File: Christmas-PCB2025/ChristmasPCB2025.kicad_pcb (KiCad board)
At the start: 2 copper layers, 20 parts, among them J1 Conn_01x08, Q1 2N7002_C306856

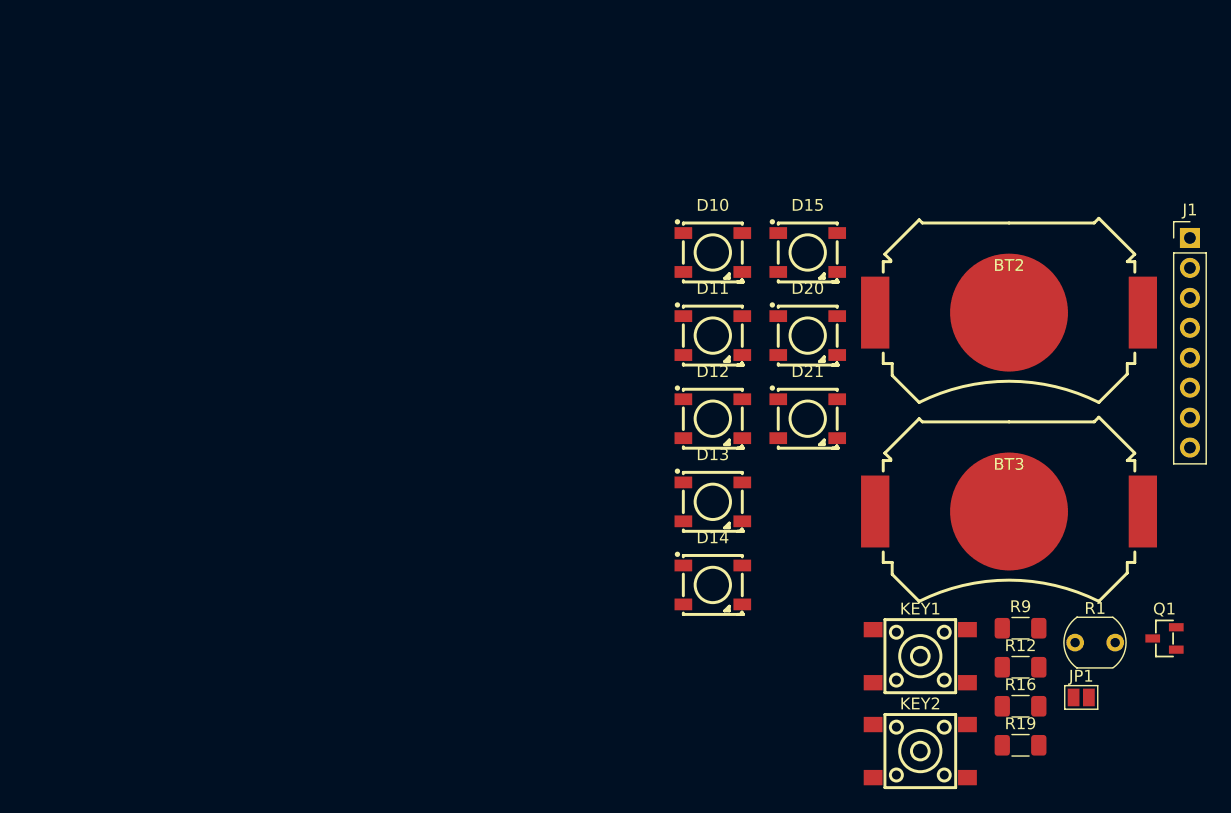
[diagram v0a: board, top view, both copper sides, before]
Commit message: removed many unnecessary components
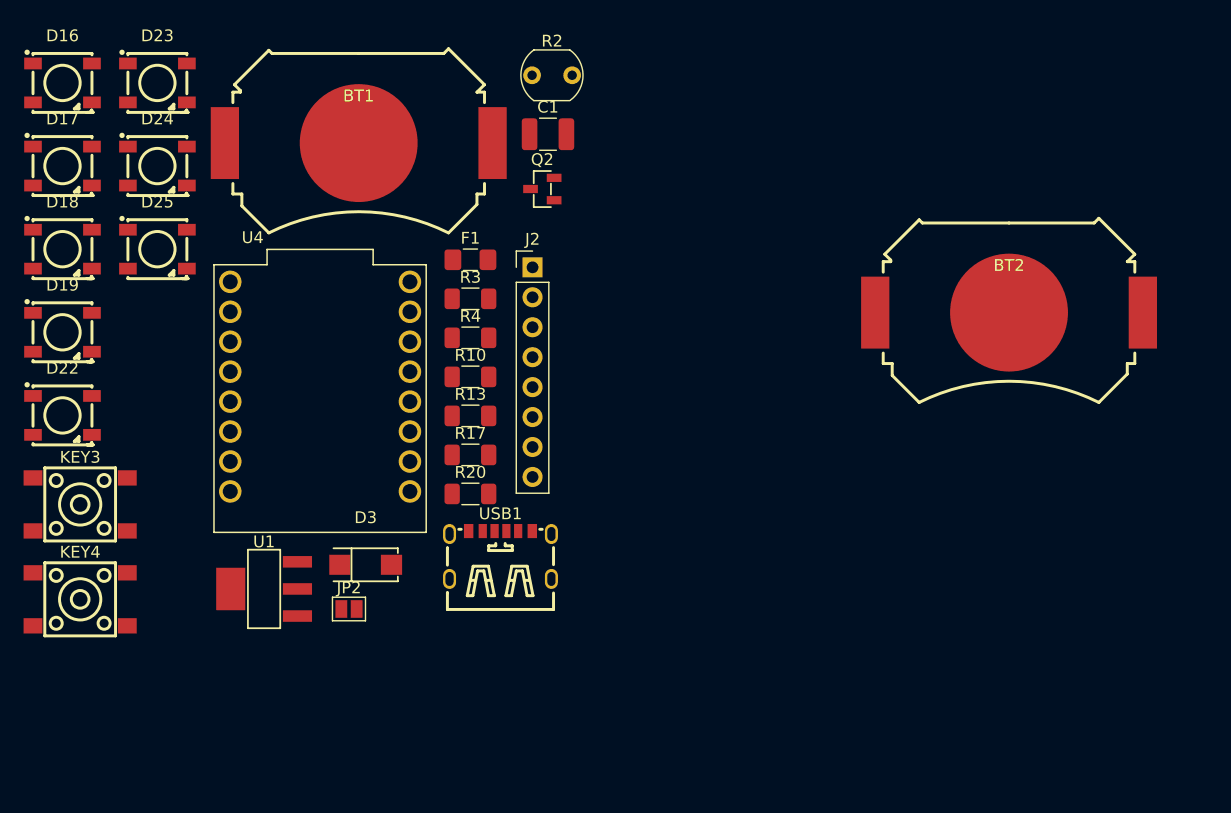
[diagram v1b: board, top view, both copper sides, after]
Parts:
- removed BT3: MY-2032-12, easyeda2kicad:BAT-SMD_MY-2032-12
- removed D10, D11, D12, D13, D14, D15, D20, D21: WS2812B, easyeda2kicad:LED-SMD_4P-L5.0-W5.0-BL_TC5050RGB
- removed J1: Conn_01x08, Connector_PinHeader_2.54mm:PinHeader_1x08_P2.54mm_Vertical
- removed JP1: SolderJumper_2_Open, Jumper:SolderJumper-2_P1.3mm_Open_Pad1.0x1.5mm
- removed KEY1, KEY2: DTSM-61R-V-T/R, easyeda2kicad:KEY-SMD_4P-L6.2-W6.2-P4.50-LS9.0
- removed Q1: 2N7002_C306856, easyeda2kicad:SOT-23-3_L2.9-W1.3-P1.90-LS2.4-BR
- removed R1: LDR07, OptoDevice:R_LDR_5.1x4.3mm_P3.4mm_Vertical
- removed R12, R19: 200, Resistor_SMD:R_1206_3216Metric_Pad1.30x1.75mm_HandSolder
- removed R16: 5k, Resistor_SMD:R_1206_3216Metric_Pad1.30x1.75mm_HandSolder
- removed R9: 10k, Resistor_SMD:R_1206_3216Metric_Pad1.30x1.75mm_HandSolder
- added BT1: MY-2032-12, easyeda2kicad:BAT-SMD_MY-2032-12, F.Cu at (44.2, 35.0)
- added C1: 47uF 10V, Capacitor_SMD:C_1210_3225Metric_Pad1.33x2.70mm_HandSolder, F.Cu at (60.2, 34.3)
- added D16: WS2812B, easyeda2kicad:LED-SMD_4P-L5.0-W5.0-BL_TC5050RGB, F.Cu at (19.0, 29.9)
- added D17: WS2812B, easyeda2kicad:LED-SMD_4P-L5.0-W5.0-BL_TC5050RGB, F.Cu at (19.0, 37.0)
- added D18: WS2812B, easyeda2kicad:LED-SMD_4P-L5.0-W5.0-BL_TC5050RGB, F.Cu at (19.0, 44.0)
- added D19: WS2812B, easyeda2kicad:LED-SMD_4P-L5.0-W5.0-BL_TC5050RGB, F.Cu at (19.0, 51.1)
- added D22: WS2812B, easyeda2kicad:LED-SMD_4P-L5.0-W5.0-BL_TC5050RGB, F.Cu at (19.0, 58.1)
- added D23: WS2812B, easyeda2kicad:LED-SMD_4P-L5.0-W5.0-BL_TC5050RGB, F.Cu at (27.1, 29.9)
- added D24: WS2812B, easyeda2kicad:LED-SMD_4P-L5.0-W5.0-BL_TC5050RGB, F.Cu at (27.1, 37.0)
- added D25: WS2812B, easyeda2kicad:LED-SMD_4P-L5.0-W5.0-BL_TC5050RGB, F.Cu at (27.1, 44.0)
- added D3: 1N5819_C437199, easyeda2kicad:SMA_L4.4-W2.6-LS5.0-RD, F.Cu at (44.7, 70.8)
- added F1: Fuse_Small 2A, Fuse:Fuse_1206_3216Metric_Pad1.42x1.75mm_HandSolder, F.Cu at (53.6, 44.9)
- added J2: Conn_01x08, Connector_PinHeader_2.54mm:PinHeader_1x08_P2.54mm_Vertical, F.Cu at (58.9, 45.6)
- added JP2: SolderJumper_2_Open, Jumper:SolderJumper-2_P1.3mm_Open_Pad1.0x1.5mm, F.Cu at (43.3, 74.5)
- added KEY3: DTSM-61R-V-T/R, easyeda2kicad:KEY-SMD_4P-L6.2-W6.2-P4.50-LS9.0, F.Cu at (20.5, 65.7)
- added KEY4: DTSM-61R-V-T/R, easyeda2kicad:KEY-SMD_4P-L6.2-W6.2-P4.50-LS9.0, F.Cu at (20.5, 73.7)
- added Q2: 2N7002_C306856, easyeda2kicad:SOT-23-3_L2.9-W1.3-P1.90-LS2.4-BR, F.Cu at (59.7, 38.9)
- added R10: 10k, Resistor_SMD:R_1206_3216Metric_Pad1.30x1.75mm_HandSolder, F.Cu at (53.6, 54.9)
- added R13: 200, Resistor_SMD:R_1206_3216Metric_Pad1.30x1.75mm_HandSolder, F.Cu at (53.6, 58.2)
- added R17: 5k, Resistor_SMD:R_1206_3216Metric_Pad1.30x1.75mm_HandSolder, F.Cu at (53.6, 61.5)
- added R2: LDR07, OptoDevice:R_LDR_5.1x4.3mm_P3.4mm_Vertical, F.Cu at (58.9, 29.3)
- added R20: 200, Resistor_SMD:R_1206_3216Metric_Pad1.30x1.75mm_HandSolder, F.Cu at (53.6, 64.8)
- added R3: 5k1, Resistor_SMD:R_1206_3216Metric_Pad1.30x1.75mm_HandSolder, F.Cu at (53.6, 48.2)
- added R4: 5k1, Resistor_SMD:R_1206_3216Metric_Pad1.30x1.75mm_HandSolder, F.Cu at (53.6, 51.5)
- added U1: AMS1117-3.3_C347222, easyeda2kicad:SOT-223-4_L6.5-W3.5-P2.30-LS7.0-BR, F.Cu at (36.1, 72.8)
- added U4: ESP32-C3_SUPERMINI_TH, custom:MODULE_ESP32-C3_SUPERMINI, F.Cu at (40.9, 56.7)
- added USB1: TYPE-C 6P(073), easyeda2kicad:TYPE-C-SMD_TYPE-C-6P_5, F.Cu at (56.2, 70.0)
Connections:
- BT2 pad 1: +5V -> Net-(BT1-Pad2)
- BT2 pad 2: Net-(BT2-Pad2) -> GND

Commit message: added new design types
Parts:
- removed D16, D17, D18, D19, D22, D23, D24, D25: WS2812B, easyeda2kicad:LED-SMD_4P-L5.0-W5.0-BL_TC5050RGB
- removed J2: Conn_01x08, Connector_PinHeader_2.54mm:PinHeader_1x08_P2.54mm_Vertical
- removed JP2: SolderJumper_2_Open, Jumper:SolderJumper-2_P1.3mm_Open_Pad1.0x1.5mm
- removed KEY3, KEY4: DTSM-61R-V-T/R, easyeda2kicad:KEY-SMD_4P-L6.2-W6.2-P4.50-LS9.0
- removed Q2: 2N7002_C306856, easyeda2kicad:SOT-23-3_L2.9-W1.3-P1.90-LS2.4-BR
- removed R13, R20: 200, Resistor_SMD:R_1206_3216Metric_Pad1.30x1.75mm_HandSolder
- removed R17: 5k, Resistor_SMD:R_1206_3216Metric_Pad1.30x1.75mm_HandSolder
- removed U4: ESP32-C3_SUPERMINI_TH, custom:MODULE_ESP32-C3_SUPERMINI
- removed USB1: TYPE-C 6P(073), easyeda2kicad:TYPE-C-SMD_TYPE-C-6P_5
- added BATT+: ~, TestPoint:TestPoint_Pad_D3.0mm, F.Cu at (407.5, 89.2)
- added BATT+1: ~, TestPoint:TestPoint_Pad_D3.0mm, F.Cu at (87.9, 18.9)
- added BATT-: TestPoint_Alt, TestPoint:TestPoint_Pad_D3.0mm, F.Cu at (414.1, 89.2)
- added BATT-1: TestPoint_Alt, TestPoint:TestPoint_Pad_D3.0mm, F.Cu at (87.9, 23.9)
- added BATTPACK1, BATTPACK2: Batteryplaceholder, MountingHole:MountingHole_2.1mm, F.Cu at (338.5, 67.8)
- added BUTTON1: DTSM-61R-V-T/R, easyeda2kicad:KEY-SMD_4P-L6.2-W6.2-P4.50-LS9.0, B.Cu at (410.1, 75.9)
- added BUTTON2: DTSM-61R-V-T/R, easyeda2kicad:KEY-SMD_4P-L6.2-W6.2-P4.50-LS9.0, B.Cu at (305.2, 66.6)
- added C2: 47uF 10V, Capacitor_SMD:C_1210_3225Metric_Pad1.33x2.70mm_HandSolder, F.Cu at (386.7, 117.4)
- added C3: 100nF 50V, Capacitor_SMD:C_1210_3225Metric_Pad1.33x2.70mm_HandSolder, F.Cu at (382.1, 117.4)
- added C4: 10uF 25V, Capacitor_SMD:C_1210_3225Metric_Pad1.33x2.70mm_HandSolder, F.Cu at (382.0, 110.5)
- added D1: SM712_SOT23, Package_TO_SOT_SMD:SOT-23, F.Cu at (87.6, 32.0)
- added D3: SM712_SOT23, Package_TO_SOT_SMD:SOT-23, F.Cu at (380.6, 91.8)
- added D4: SM712_SOT23, Package_TO_SOT_SMD:SOT-23, F.Cu at (377.6, 93.7)
- added D5: 1N5819_C437199, easyeda2kicad:SMA_L4.4-W2.6-LS5.0-RD, F.Cu at (400.7, 103.0)
- added F2: Fuse_Small 2A, Fuse:Fuse_1206_3216Metric_Pad1.42x1.75mm_HandSolder, F.Cu at (398.9, 109.2)
- added G***: LOGO, project_footprints:tree_shadow, F.Cu at (430.3, -91.6)
- added G***: LOGO, project_footprints:frosty-shadow, F.Cu at (280.5, -74.6)
- added G***: LOGO, project_footprints:frosty-body, F.Cu at (280.8, -75.0)
- added G***: LOGO, project_footprints:frosty-carrot, F.Cu at (281.0, -75.6)
- added G***: LOGO, project_footprints:ornament_reflect, F.Cu at (137.9, -70.6)
- added G***: LOGO, project_footprints:tree_star, F.Cu at (428.5, -98.4)
- added G***: LOGO, project_footprints:ornament_shadow, F.Cu at (135.4, -68.7)
- added G***: LOGO, project_footprints:ornament_crown, F.Cu at (135.1, -69.5)
- added GND: TestPoint_Probe, TestPoint:TestPoint_Pad_D2.0mm, F.Cu at (358.5, 92.0)
- added HDR1: Conn_01x08, Connector_PinHeader_2.54mm:PinHeader_1x08_P2.54mm_Vertical, B.Cu at (401.5, 73.0)
- added J1: Conn_01x08, Connector_PinHeader_2.54mm:PinHeader_1x08_P2.54mm_Vertical_SMD_Pin1Left, F.Cu at (75.5, 27.6)
- added JP1: SolderJumper_2_Open, Jumper:SolderJumper-2_P1.3mm_Open_Pad1.0x1.5mm, F.Cu at (87.3, 36.0)
- added LDR1: LDR07, OptoDevice:R_LDR_5.1x4.3mm_P3.4mm_Vertical, B.Cu at (397.8, 60.9)
- added LED1: WS2812B, easyeda2kicad:LED-SMD_4P-L5.0-W5.0-BL_TC5050RGB, B.Cu at (386.9, 32.6)
- added LED2: WS2812B, easyeda2kicad:LED-SMD_4P-L5.0-W5.0-BL_TC5050RGB, B.Cu at (337.2, 33.5)
- added LED3: WS2812B, easyeda2kicad:LED-SMD_4P-L5.0-W5.0-BL_TC5050RGB, B.Cu at (409.5, 64.7)
- added LED4: WS2812B, easyeda2kicad:LED-SMD_4P-L5.0-W5.0-BL_TC5050RGB, B.Cu at (308.9, 51.7)
- added LED5: WS2812B, easyeda2kicad:LED-SMD_4P-L5.0-W5.0-BL_TC5050RGB, B.Cu at (407.3, 97.0)
- added LED6: WS2812B, easyeda2kicad:LED-SMD_4P-L5.0-W5.0-BL_TC5050RGB, B.Cu at (307.0, 83.5)
- added LED7: WS2812B, easyeda2kicad:LED-SMD_4P-L5.0-W5.0-BL_TC5050RGB, B.Cu at (379.3, 110.5)
- added LED8: WS2812B, easyeda2kicad:LED-SMD_4P-L5.0-W5.0-BL_TC5050RGB, B.Cu at (346.6, 108.4)
- added LS1: KSSGK4B16-20, CustomPartsCRT:KSSGK4B16-20, B.Cu at (349.8, 57.5)
- added Q1: 2N7002_C306856, easyeda2kicad:SOT-23-3_L2.9-W1.3-P1.90-LS2.4-BR, F.Cu at (109.0, 129.0)
- added R11: 200, Resistor_SMD:R_1206_3216Metric_Pad1.30x1.75mm_HandSolder, F.Cu at (107.3, 134.9)
- added R12: 10k, Resistor_SMD:R_1206_3216Metric_Pad1.30x1.75mm_HandSolder, F.Cu at (110.7, 134.9)
- added R14: 200, Resistor_SMD:R_1206_3216Metric_Pad1.30x1.75mm_HandSolder, F.Cu at (353.2, 112.0)
- added R15: 10k, Resistor_SMD:R_1206_3216Metric_Pad1.30x1.75mm_HandSolder, F.Cu at (388.2, 111.4)
- added R2: 10k, Resistor_SMD:R_1206_3216Metric_Pad1.30x1.75mm_HandSolder, F.Cu at (82.4, 18.0)
- added R4: 10k, Resistor_SMD:R_1206_3216Metric_Pad1.30x1.75mm_HandSolder, F.Cu at (82.4, 24.6)
- added R5: 100, Resistor_SMD:R_1206_3216Metric_Pad1.30x1.75mm_HandSolder, F.Cu at (82.4, 27.9)
- added R8: 5k, Resistor_SMD:R_1206_3216Metric_Pad1.30x1.75mm_HandSolder, F.Cu at (396.0, 66.0)
- added R9: 10k, Resistor_SMD:R_1206_3216Metric_Pad1.30x1.75mm_HandSolder, F.Cu at (111.2, 119.9)
- added REF**: Pin_Header_Straight_1x01, idlehands_footprints:frosty-eye, F.Cu at (288.4, -98.9)
- added REF**: MountingHole_2.5mm, idlehands_footprints:MountingHole_2.5mm_NO, B.Cu at (135.1, -113.0)
- added REF**: MountingHole_2.5mm, idlehands_footprints:MountingHole_2.5mm_NO, B.Cu at (280.7, -124.6)
- added REF**: MountingHole_2.5mm, idlehands_footprints:MountingHole_2.5mm_NO, B.Cu at (428.7, -142.0)
- added RXD: TestPoint_Probe, TestPoint:TestPoint_Pad_D2.0mm, F.Cu at (354.4, 92.0)
- added TXD: TestPoint_Probe, TestPoint:TestPoint_Pad_D2.0mm, F.Cu at (350.4, 91.9)
- added USB+: TestPoint_Probe, TestPoint:TestPoint_Pad_D2.0mm, F.Cu at (365.7, 94.6)
- added USB-: TestPoint_Probe, TestPoint:TestPoint_Pad_D2.0mm, F.Cu at (370.8, 94.6)
- D1: renamed from D3; value 1N5819_C437199 -> WS2812B
- F1: value Fuse_Small 2A -> Resetable fuse 0.75A
- R1: renamed from R2; value LDR07 -> 10k; footprint OptoDevice:R_LDR_5.1x4.3mm_P3.4mm_Vertical -> Resistor_SMD:R_1206_3216Metric_Pad1.30x1.75mm_HandSolder
- R3: value 5k1 -> 200
- R7: renamed from R4; value 5k1 -> 5k
- U1: value AMS1117-3.3_C347222 -> ESP32-C3_SUPERMINI_TH; footprint easyeda2kicad:SOT-223-4_L6.5-W3.5-P2.30-LS7.0-BR -> custom:MODULE_ESP32-C3_SUPERMINI
- moved C1 339.2 mm to (392.2, 103.5), turned to 180 degrees
- moved BT1 309.1 mm to (351.6, 66.6), turned to 180 degrees
- moved BT2 278.7 mm to (377.5, 66.6), turned to 180 degrees
- moved U1 243.9 mm to (274.2, 126.2)
- moved R10 84.2 mm to (107.0, 119.9), turned to -90 degrees
- moved R3 39.4 mm to (82.4, 21.3)
- moved D1 21.6 mm to (66.3, 70.5)
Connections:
- BT1 pad 1: Net-(D3-A) -> Net-(BT1-Pad2)
- BT1 pad 2: Net-(BT1-Pad2) -> GND
- BT2 pad 1: Net-(BT1-Pad2) -> Net-(D1-A)
- BT2 pad 2: GND -> Net-(BT1-Pad2)
- D1 pad 1: Net-(D3-C) -> +5V
- D1 pad 2: Net-(D3-A) -> Net-(D3-DOUT)
- F1 pad 2: Net-(D3-C) -> Net-(D1-C)
- R1 pad 1: +3V3 -> BATT_V
- R1 pad 2: Net-(U4-GPIO2) -> GND
- R10 pad 1: GND -> Net-(D1-A)
- R10 pad 2: BUZZ -> BATT_V
- R3 pad 1: GND -> Net-(D2-DIN)
- R3 pad 2: Net-(USB1-CC2) -> RGB
- R7 pad 1: GND -> Net-(U1-GPIO2)
- R7 pad 2: Net-(USB1-CC1) -> GND
- U1 pad 1: +3V3 -> unconnected-(U1-GPIO1-Pad1)
- U1 pad 2: +3V3 -> Net-(U1-GPIO2)
- U1 pad 3: +5V -> unconnected-(U1-GPIO3-Pad3)
- U1 pad 4: GND -> Net-(U1-GPIO4)
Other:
- board outline added: 388.8 x 303.7 mm
- board text added: "3.3V"
- board text added: "AAA"
- board text added: "BATTERY_V"
- board text added: "BUZZER_CTRL"
- board text added: "CR2032"
- board text added: "GND"
- board text added: "GPIO HDR"
- board text added: "INT"
- board text added: "Mounting Hole"
- board text added: "NC"
- board text added: "SCL"
- board text added: "SDA"
- board text added: "SDO"
- board text added: "Wear me! Mount me! Stand me! Dangle me!"

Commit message: settled on ornament design
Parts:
- removed BATT+: ~, TestPoint:TestPoint_Pad_D3.0mm
- removed BATT-: TestPoint_Alt, TestPoint:TestPoint_Pad_D3.0mm
- removed BATTPACK2: Batteryplaceholder, MountingHole:MountingHole_2.1mm
- removed C1, C2: 47uF 10V, Capacitor_SMD:C_1210_3225Metric_Pad1.33x2.70mm_HandSolder
- removed C3: 100nF 50V, Capacitor_SMD:C_1210_3225Metric_Pad1.33x2.70mm_HandSolder
- removed C4: 10uF 25V, Capacitor_SMD:C_1210_3225Metric_Pad1.33x2.70mm_HandSolder
- removed D3, D4: SM712_SOT23, Package_TO_SOT_SMD:SOT-23
- removed D5: 1N5819_C437199, easyeda2kicad:SMA_L4.4-W2.6-LS5.0-RD
- removed F2: Fuse_Small 2A, Fuse:Fuse_1206_3216Metric_Pad1.42x1.75mm_HandSolder
- removed the G*** at (430.3, -91.6)
- removed the G*** at (280.5, -74.6)
- removed the G*** at (280.8, -75.0)
- removed the G*** at (281.0, -75.6)
- removed the G*** at (428.5, -98.4)
- removed GND, RXD, TXD, USB+, USB-: TestPoint_Probe, TestPoint:TestPoint_Pad_D2.0mm
- removed HDR1: Conn_01x08, Connector_PinHeader_2.54mm:PinHeader_1x08_P2.54mm_Vertical
- removed R10, R12, R15, R9: 10k, Resistor_SMD:R_1206_3216Metric_Pad1.30x1.75mm_HandSolder
- removed R11, R14: 200, Resistor_SMD:R_1206_3216Metric_Pad1.30x1.75mm_HandSolder
- removed R8: 5k, Resistor_SMD:R_1206_3216Metric_Pad1.30x1.75mm_HandSolder
- removed the REF** at (288.4, -98.9)
- removed the REF** at (135.1, -113.0)
- removed the REF** at (280.7, -124.6)
- removed the REF** at (428.7, -142.0)
- added BATTPACK1: Batteryplaceholder, MountingHole:MountingHole_2.1mm, B.Cu at (160.0, -66.8)
- added D2: SM712_SOT23, Package_TO_SOT_SMD:SOT-23, F.Cu at (197.9, -79.5)
- added REF**: MountingHole_2.5mm, idlehands_footprints:MountingHole_2.5mm_NO, B.Cu at (135.1, -112.8)
- D1: value WS2812B -> 1N5819_C437199
- D1: value SM712_SOT23 -> 1N5819_C437199
- U1: moved to B.Cu
- moved LED2 230.0 mm to (144.4, -91.8), turned to 180 degrees
- moved U1 214.1 mm to (135.0, -36.5)
- moved G*** 0.26 mm to (135.1, -69.2)
- moved G*** 0.26 mm to (137.9, -70.3)
- moved G*** 0.26 mm to (135.4, -68.5)
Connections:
- BT1 pad 1: Net-(BT1-Pad2) -> Net-(D1-A)
- BT1 pad 2: GND -> Net-(BT1-Pad2)
- BT2 pad 1: Net-(D1-A) -> Net-(BT1-Pad2)
- BT2 pad 2: Net-(BT1-Pad2) -> GND
- BUTTON1 pad 3: GPIO4 -> Net-(U1-GPIO4)
- BUTTON1 pad 4: GPIO4 -> Net-(U1-GPIO4)
- BUTTON2 pad 3: GPIO5 -> Net-(U1-GPIO5)
- BUTTON2 pad 4: GPIO5 -> Net-(U1-GPIO5)
- D1 pad 1: +5V -> Net-(D1-C)
- D1 pad 2: Net-(D3-DOUT) -> Net-(D1-A)
- D1 pad 1: SCL -> Net-(D1-C)
- D1 pad 2: SDA -> Net-(D1-A)
- D1 pad 3: GND -> (no net)
- LDR1 pad 2: Net-(U2-IO2) -> Net-(U1-GPIO2)
- LED1 pad 2: Net-(LED5-DOUT) -> Net-(LED1-DOUT)
- LED1 pad 4: Net-(LED4-DOUT) -> Net-(LED1-DIN)
- LED2 pad 2: Net-(LED4-DOUT) -> Net-(LED2-DOUT)
- LED2 pad 4: Net-(LED3-DOUT) -> Net-(LED1-DOUT)
- LED3 pad 2: Net-(LED6-DOUT) -> Net-(LED3-DOUT)
- LED3 pad 4: Net-(LED5-DOUT) -> Net-(LED2-DOUT)
- LED4 pad 2: Net-(LED3-DOUT) -> Net-(LED4-DOUT)
- LED4 pad 4: Net-(LED2-DOUT) -> Net-(LED3-DOUT)
- LED5 pad 2: Net-(LED7-DOUT) -> Net-(LED5-DOUT)
- LED5 pad 4: Net-(LED6-DOUT) -> Net-(LED4-DOUT)
- LED6 pad 2: Net-(LED2-DOUT) -> Net-(LED6-DOUT)
- LED6 pad 4: Net-(LED1-DOUT) -> Net-(LED5-DOUT)
- LED7 pad 2: unconnected-(LED8-DOUT-Pad2) -> Net-(LED7-DOUT)
- LED7 pad 4: Net-(LED7-DOUT) -> Net-(LED6-DOUT)
- LED8 pad 2: Net-(LED1-DOUT) -> unconnected-(LED8-DOUT-Pad2)
- LED8 pad 4: Net-(LED1-DIN) -> Net-(LED7-DOUT)
- R3 pad 1: Net-(D2-DIN) -> Net-(LED1-DIN)
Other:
- board size 388.8 x 303.7 mm -> 134.3 x 272.6 mm

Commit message: finished playfull routing
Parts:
- removed BATTPACK1: Batteryplaceholder, MountingHole:MountingHole_2.1mm
- removed BT1, BT2: MY-2032-12, easyeda2kicad:BAT-SMD_MY-2032-12
- removed the D1 at (87.6, 32.0)
- removed D2: SM712_SOT23, Package_TO_SOT_SMD:SOT-23
- removed J1: Conn_01x08, Connector_PinHeader_2.54mm:PinHeader_1x08_P2.54mm_Vertical_SMD_Pin1Left
- BATT+: renamed from BATT+1; moved to B.Cu
- BATT-: renamed from BATT-1; moved to B.Cu
- D1, F1, JP1, Q1, R1, R2, R3, R4, R5, R7: moved to B.Cu
- LED1: renamed from LED2; footprint easyeda2kicad:LED-SMD_4P-L5.0-W5.0-BL_TC5050RGB -> CustomLed:LED_WS2812B_PLCC4_5.0x5.0mm_P3.2mm
- LED2: renamed from LED4; footprint easyeda2kicad:LED-SMD_4P-L5.0-W5.0-BL_TC5050RGB -> CustomLed:LED_WS2812B_PLCC4_5.0x5.0mm_P3.2mm
- LED3, LED6: footprint easyeda2kicad:LED-SMD_4P-L5.0-W5.0-BL_TC5050RGB -> CustomLed:LED_WS2812B_PLCC4_5.0x5.0mm_P3.2mm
- LED4: renamed from LED8; footprint easyeda2kicad:LED-SMD_4P-L5.0-W5.0-BL_TC5050RGB -> CustomLed:LED_WS2812B_PLCC4_5.0x5.0mm_P3.2mm
- LED5: renamed from LED7; footprint easyeda2kicad:LED-SMD_4P-L5.0-W5.0-BL_TC5050RGB -> CustomLed:LED_WS2812B_PLCC4_5.0x5.0mm_P3.2mm
- LED7: renamed from LED5; footprint easyeda2kicad:LED-SMD_4P-L5.0-W5.0-BL_TC5050RGB -> CustomLed:LED_WS2812B_PLCC4_5.0x5.0mm_P3.2mm
- LED8: renamed from LED1; footprint easyeda2kicad:LED-SMD_4P-L5.0-W5.0-BL_TC5050RGB -> CustomLed:LED_WS2812B_PLCC4_5.0x5.0mm_P3.2mm
- moved LDR1 273.6 mm to (125.0, 82.8), turned to -140 degrees
- moved LED3 267.8 mm to (146.1, 113.0)
- moved LED5 263.3 mm to (116.0, 113.9)
- moved LED8 250.5 mm to (140.7, 79.2)
- moved LED7 248.1 mm to (161.4, 130.2)
- moved BUTTON1 237.1 mm to (174.0, 97.7)
- moved LED4 214.7 mm to (132.1, 98.4)
- moved LS1 199.6 mm to (151.6, 81.0), turned to -90 degrees
- moved BUTTON2 193.5 mm to (114.2, 97.6)
- moved LED6 186.8 mm to (126.4, 131.5), turned to 150 degrees
- moved LED1 182.2 mm to (162.0, 89.5)
- moved BATTPACK1: 172.3 mm to (169.7, 105.2)
- moved G*** 172.2 mm to (144.2, 103.5)
- moved G*** 172.2 mm to (143.9, 102.7)
- moved G*** 172.2 mm to (146.7, 101.7)
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- renumbered BATTPACK1 to BATTPACK1:
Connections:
- net SCL renamed Net-(JP1-B)
- LED1 pad 2: Net-(LED2-DOUT) -> Net-(LED1-DOUT)
- LED1 pad 4: Net-(LED1-DOUT) -> Net-(LED1-DIN)
- LED2 pad 2: Net-(LED4-DOUT) -> Net-(LED2-DOUT)
- LED2 pad 4: Net-(LED3-DOUT) -> Net-(LED1-DOUT)
- LED4 pad 2: unconnected-(LED8-DOUT-Pad2) -> Net-(LED4-DOUT)
- LED4 pad 4: Net-(LED7-DOUT) -> Net-(LED3-DOUT)
- LED5 pad 2: Net-(LED7-DOUT) -> Net-(LED5-DOUT)
- LED5 pad 4: Net-(LED6-DOUT) -> Net-(LED4-DOUT)
- LED7 pad 2: Net-(LED5-DOUT) -> Net-(LED7-DOUT)
- LED7 pad 4: Net-(LED4-DOUT) -> Net-(LED6-DOUT)
- LED8 pad 2: Net-(LED1-DOUT) -> unconnected-(LED8-DOUT-Pad2)
- LED8 pad 4: Net-(LED1-DIN) -> Net-(LED7-DOUT)
- U1 pad 20: INT -> unconnected-(U1-GPIO20-Pad20)
- U1 pad 21: SDO -> unconnected-(U1-GPIO21-Pad21)
- U1 pad 3: unconnected-(U1-GPIO3-Pad3) -> RGB
- U1 pad 8: SDA -> unconnected-(U1-GPIO8-Pad8)
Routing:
- net +5V: track 0.00 -> 212.4 mm, vias 0 -> 6
- net +3V3: track 0.00 -> 117.4 mm, vias 0 -> 3
- net Net-(LED7-DOUT): track 0.00 -> 80.1 mm, vias 0 -> 2
- net Net-(U1-GPIO2): track 0.00 -> 76.2 mm, vias 0 -> 2
- net RGB: track 0.00 -> 67.0 mm, vias 0 -> 2
- net Net-(U1-GPIO5): track 0.00 -> 65.2 mm, vias 0 -> 2
- net Net-(U1-GPIO4): track 0.00 -> 60.4 mm, vias 0 -> 2
- net Net-(Q1-D): track 0.00 -> 57.4 mm, vias 0 -> 2
- net BUZZ: track 0.00 -> 53.3 mm, vias 0 -> 2
- net Net-(LED4-DOUT): track 0.00 -> 51.9 mm
- net Net-(LED6-DOUT): track 0.00 -> 36.8 mm, vias 0 -> 2
- net Net-(LED2-DOUT): track 0.00 -> 34.6 mm
- net BATT_V: track 0.00 -> 34.5 mm, vias 0 -> 2
- net GND: track 0.00 -> 29.7 mm, vias 0 -> 20
- net Net-(LED1-DOUT): track 0.00 -> 29.2 mm, vias 0 -> 2
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- added copper zone on B.Cu, net GND
- added copper zone on F.Cu, net GND
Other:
- board size 134.3 x 272.6 mm -> 76.2 x 93.3 mm
- board text added: "0"
- board text added: "21"
- board text added: "ESP32-C3 SuperMini"
- board text removed: "3.3V"
- board text removed: "BATTERY_V"
- board text removed: "BUZZER_CTRL"
- board text removed: "CR2032"
- board text removed: "GND"
- board text removed: "GPIO HDR"
- board text removed: "INT"
- board text removed: "Mounting Hole"
- board text removed: "NC"
- board text removed: "SCL"
- board text removed: "SDA"
- board text removed: "SDO"
- board text removed: "Wear me! Mount me! Stand me! Dangle me!"
